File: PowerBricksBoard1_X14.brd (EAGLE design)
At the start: 76.2 x 53.3 mm, 16 parts, among them J1 PESC-02-12-02-01-X-VT-LC(BRIC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

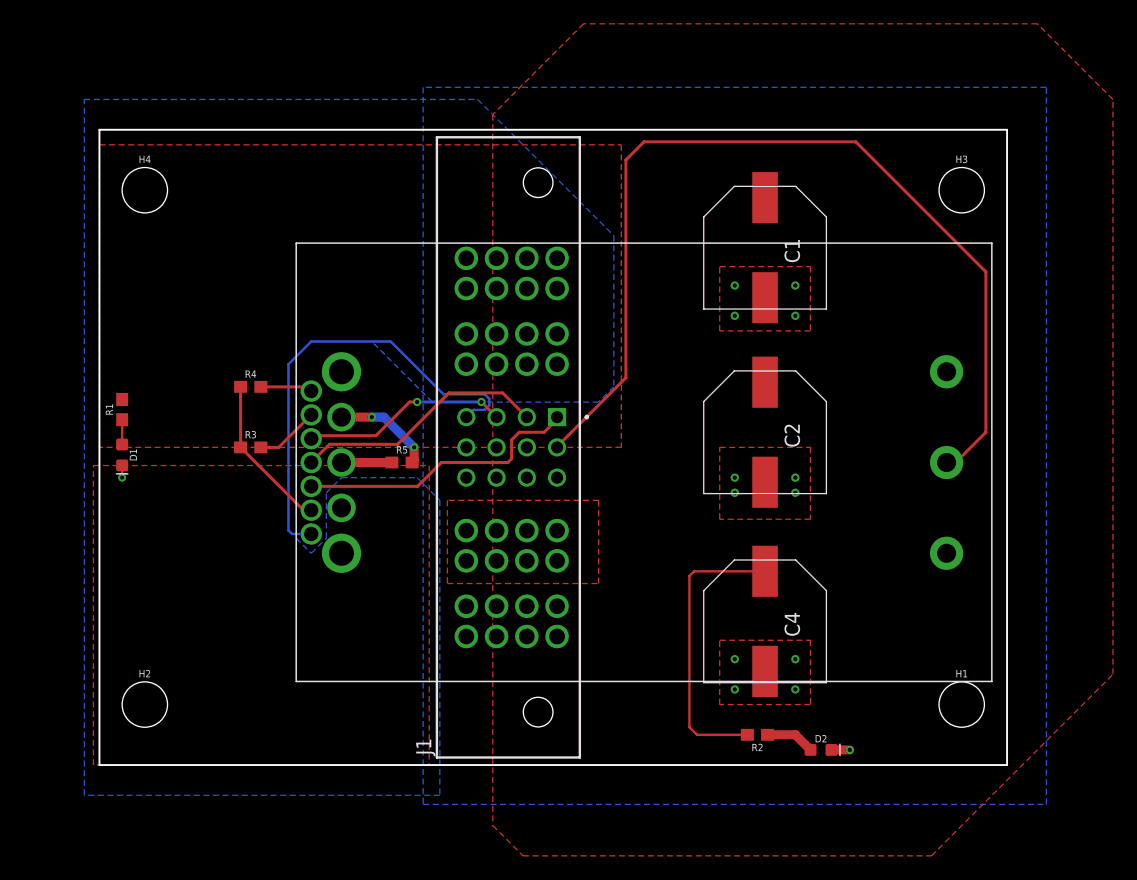
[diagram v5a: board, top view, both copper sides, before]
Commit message: Added Silkscreen
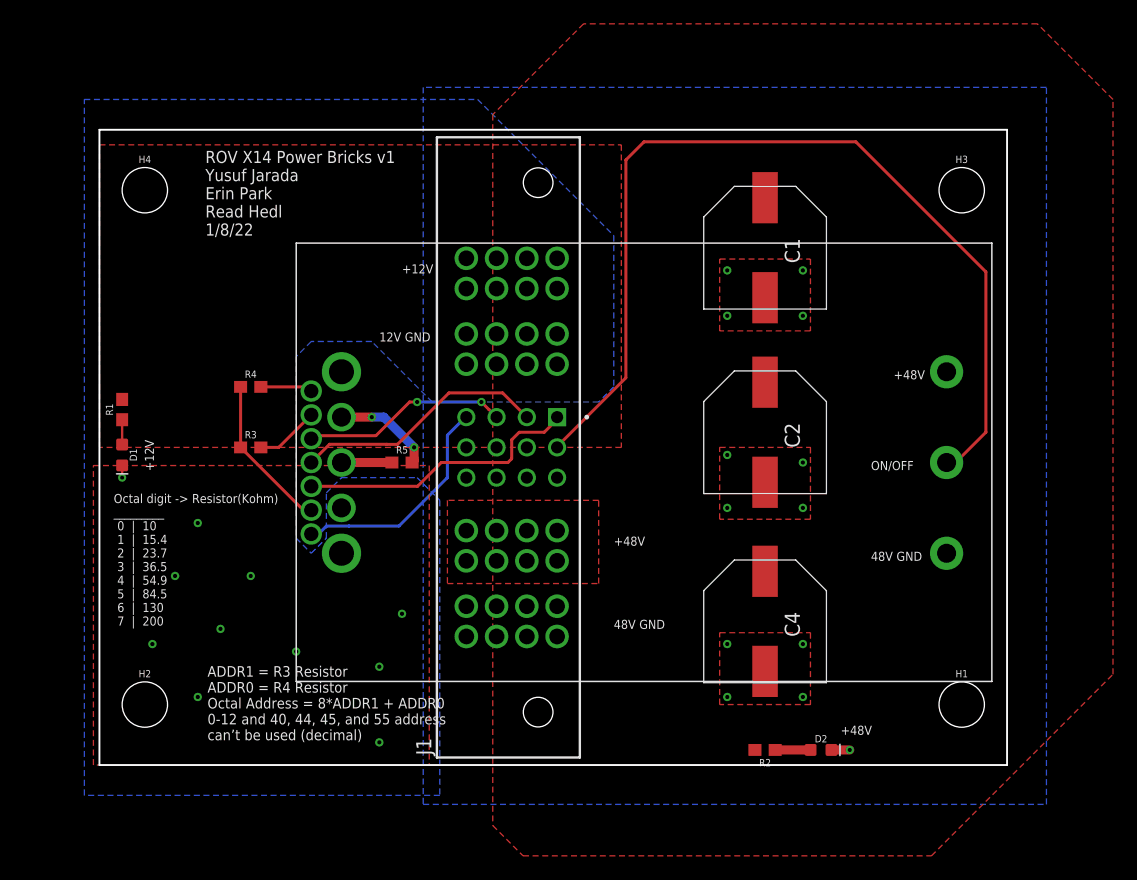
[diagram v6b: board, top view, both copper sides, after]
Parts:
- moved R2 1.42 mm to (55.9, 0.00)
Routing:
- net 48V: track 24.3 -> 0.00 mm
- net C2: track 38.5 -> 19.2 mm
- net N$2: track 4.13 -> 2.97 mm
- net 12_GND: vias 1 -> 11
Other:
- board text added: "+12V"
- board text added: "+48V"
- board text added: "12V GND"
- board text added: "48V GND"
- board text added: "ADDR1 = R3 Resistor ADDR0 = R4 Resistor Octal Address = 8*ADDR1 + ADDR0 0-12 and 40, 44, 45, and 55 address can’t be used (decimal)"
- board text added: "ON/OFF"
- board text added: "Octal digit -> Resistor(Kohm) _________ 0 | 10 1 | 15.4 2 | 23.7 3 | 36.5 4 | 54.9 5 | 84.5 6 | 130 7 | 200"
- board text added: "ROV X14 Power Bricks v1 Yusuf Jarada Erin Park Read Hedl 1/8/22"
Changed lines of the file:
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@@
 <?xml version="1.0" encoding="utf-8"?>
 <!DOCTYPE eagle SYSTEM "eagle.dtd">
-<eagle version="9.6.2">
+<eagle version="9.5.0">
 <drawing>
 <settings>
@@
 <wire x1="76.2" y1="52.07" x2="0" y2="52.07" width="0" layer="20"/>
 <wire x1="0" y1="52.07" x2="0" y2="-1.27" width="0" layer="20"/>
+<text x="8.89" y="43.18" size="1.016" layer="25">ROV X14 Power Bricks v1
+Yusuf Jarada
+Erin Park
+Read Hedl
+1/8/22</text>
+<text x="66.675" y="31.115" size="0.762" layer="25">+48V</text>
+<text x="64.77" y="15.875" size="0.762" layer="25">48V GND</text>
+<text x="64.77" y="23.495" size="0.762" layer="25">ON/OFF</text>
+<text x="25.4" y="40.005" size="0.762" layer="25">+12V</text>
+<text x="43.18" y="17.145" size="0.762" layer="25">+48V</text>
+<text x="43.18" y="10.16" size="0.762" layer="25">48V GND</text>
+<text x="23.495" y="34.29" size="0.762" layer="25">12V GND</text>
+<text x="62.23" y="1.27" size="0.762" layer="25">+48V</text>
+<text x="3.81" y="26.035" size="0.762" layer="25" rot="R270">+12V</text>
+<text x="9.0678" y="0.8128" size="0.889" layer="25">ADDR1 = R3 Resistor
+ADDR0 = R4 Resistor
+Octal Address = 8*ADDR1 + ADDR0
+0-12 and 40, 44, 45, and 55 address
+can’t be used (decimal)</text>
+<text x="1.1938" y="10.4394" size="0.762" layer="25">Octal digit -&gt; Resistor(Kohm)
+_________
+ 0  |  10
+ 1  |  15.4
+ 2  |  23.7
+ 3  |  36.5
+ 4  |  54.9
+ 5  |  84.5
+ 6  |  130
+ 7  |  200</text>
 </plain>
 <attributes>
@@
 <attribute name="VALUE" x="2.667" y="28.575" size="0.6096" layer="27" font="vector" ratio="20" rot="R90" align="top-center"/>
 </element>
-<element name="R2" library="SparkFun-Resistors" library_urn="urn:adsk.eagle:library:532" package="0603" package3d_urn="urn:adsk.eagle:package:39650/1" value="2400" x="55.245" y="1.27" smashed="yes" rot="R180">
-<attribute name="NAME" x="55.245" y="0.508" size="0.6096" layer="25" font="vector" ratio="20" rot="R180" align="bottom-center"/>
-<attribute name="PROD_ID" value=" " x="22.225" y="69.85" size="1.778" layer="27" rot="R180" display="off"/>
-<attribute name="VALUE" x="55.245" y="2.032" size="0.6096" layer="27" font="vector" ratio="20" rot="R180" align="top-center"/>
+<element name="R2" library="SparkFun-Resistors" library_urn="urn:adsk.eagle:library:532" package="0603" package3d_urn="urn:adsk.eagle:package:39650/1" value="2400" x="55.88" y="0" smashed="yes" rot="R180">
+<attribute name="NAME" x="55.88" y="-0.762" size="0.6096" layer="25" font="vector" ratio="20" rot="R180" align="bottom-center"/>
+<attribute name="PROD_ID" value=" " x="22.86" y="68.58" size="1.778" layer="27" rot="R180" display="off"/>
+<attribute name="VALUE" x="55.88" y="0.762" size="0.6096" layer="27" font="vector" ratio="20" rot="R180" align="top-center"/>
 </element>
 <element name="R3" library="SparkFun-Resistors" library_urn="urn:adsk.eagle:library:532" package="0603" package3d_urn="urn:adsk.eagle:package:39650/1" value=" " x="12.7" y="25.4" smashed="yes">
@@
 </polygon>
 <contactref element="U$2" pad="4"/>
-<polygon width="0.254" layer="1">
-<vertex x="52.07" y="9.2075"/>
-<vertex x="59.69" y="9.2075"/>
+<polygon width="0.762" layer="1">
+<vertex x="52.07" y="9.8425"/>
+<vertex x="59.69" y="9.8425"/>
 <vertex x="59.69" y="3.81"/>
 <vertex x="52.07" y="3.81"/>
 </polygon>
-<via x="53.34" y="7.62" extent="1-16" drill="0.35"/>
-<via x="58.42" y="7.62" extent="1-16" drill="0.35"/>
-<polygon width="0.254" layer="1">
-<vertex x="52.07" y="40.5765"/>
-<vertex x="59.69" y="40.5765"/>
+<via x="52.705" y="8.89" extent="1-16" drill="0.35"/>
+<via x="59.055" y="8.89" extent="1-16" drill="0.35"/>
+<polygon width="0.762" layer="1">
+<vertex x="52.07" y="41.2115"/>
+<vertex x="59.69" y="41.2115"/>
 <vertex x="59.69" y="35.179"/>
 <vertex x="52.07" y="35.179"/>
 </polygon>
-<polygon width="0.254" layer="1">
+<polygon width="0.762" layer="1">
 <vertex x="52.07" y="25.4"/>
 <vertex x="59.69" y="25.4"/>
@@
 <vertex x="52.07" y="19.3675"/>
 </polygon>
-<via x="53.34" y="21.59" extent="1-16" drill="0.35"/>
-<via x="58.42" y="21.59" extent="1-16" drill="0.35"/>
-<via x="58.42" y="22.86" extent="1-16" drill="0.35"/>
-<via x="53.34" y="22.86" extent="1-16" drill="0.35"/>
-<via x="53.34" y="36.449" extent="1-16" drill="0.35"/>
-<via x="53.34" y="38.989" extent="1-16" drill="0.35"/>
-<via x="58.42" y="38.989" extent="1-16" drill="0.35"/>
-<via x="58.42" y="36.449" extent="1-16" drill="0.35"/>
-<via x="53.34" y="5.08" extent="1-16" drill="0.35"/>
-<via x="58.42" y="5.08" extent="1-16" drill="0.35"/>
+<via x="52.705" y="20.32" extent="1-16" drill="0.35"/>
+<via x="59.055" y="20.32" extent="1-16" drill="0.35"/>
+<via x="59.055" y="24.13" extent="1-16" drill="0.35"/>
+<via x="52.705" y="24.765" extent="1-16" drill="0.35"/>
+<via x="52.705" y="36.449" extent="1-16" drill="0.35"/>
+<via x="52.705" y="40.259" extent="1-16" drill="0.35"/>
+<via x="59.055" y="40.259" extent="1-16" drill="0.35"/>
+<via x="59.055" y="36.449" extent="1-16" drill="0.35"/>
+<via x="52.705" y="4.445" extent="1-16" drill="0.35"/>
+<via x="59.055" y="4.445" extent="1-16" drill="0.35"/>
 <contactref element="J1" pad="P04_1"/>
 <contactref element="J1" pad="P04_2"/>
@@
 <contactref element="U$2" pad="10"/>
 <contactref element="J1" pad="04"/>
-<wire x1="17.78" y1="18.13" x2="16.16" y2="18.13" width="0.2032" layer="16"/>
-<wire x1="16.16" y1="18.13" x2="15.875" y2="18.415" width="0.2032" layer="16"/>
-<wire x1="15.875" y1="18.415" x2="15.875" y2="32.385" width="0.2032" layer="16"/>
-<wire x1="15.875" y1="32.385" x2="17.78" y2="34.29" width="0.2032" layer="16"/>
-<wire x1="32.3398875" y1="29.8676" x2="32.7251" y2="29.4823875" width="0.2032" layer="16"/>
-<wire x1="32.7251" y1="29.4823875" x2="32.7251" y2="28.9376125" width="0.2032" layer="16"/>
-<wire x1="32.7251" y1="28.9376125" x2="32.3398875" y2="28.5524" width="0.2032" layer="16"/>
-<wire x1="24.45" y1="34.29" x2="28.8724" y2="29.8676" width="0.2032" layer="16"/>
-<wire x1="32.3398875" y1="28.5524" x2="31.4124" y2="28.5524" width="0.2032" layer="16"/>
-<wire x1="31.4124" y1="28.5524" x2="30.8" y2="27.94" width="0.2032" layer="16"/>
-<wire x1="28.8724" y1="29.8676" x2="32.3398875" y2="29.8676" width="0.2032" layer="16"/>
-<wire x1="17.78" y1="34.29" x2="24.45" y2="34.29" width="0.2032" layer="16"/>
+<wire x1="17.78" y1="18.13" x2="18.384" y2="18.13" width="0.254" layer="16"/>
+<wire x1="20.95383125" y1="18.7898" x2="20.96003125" y2="18.796" width="0.254" layer="16"/>
+<wire x1="19.0438" y1="18.7898" x2="20.95383125" y2="18.7898" width="0.254" layer="16"/>
+<wire x1="25.146" y1="18.796" x2="29.21" y2="22.86" width="0.254" layer="16"/>
+<wire x1="29.21" y1="22.86" x2="29.21" y2="26.416" width="0.254" layer="16"/>
+<wire x1="29.21" y1="26.416" x2="30.734" y2="27.94" width="0.254" layer="16"/>
+<wire x1="30.734" y1="27.94" x2="30.8" y2="27.94" width="0.254" layer="16"/>
+<wire x1="18.384" y1="18.13" x2="19.0438" y2="18.7898" width="0.254" layer="16"/>
+<wire x1="20.96003125" y1="18.796" x2="25.146" y2="18.796" width="0.254" layer="16"/>
 </signal>
 <signal name="12_GND">
@@
 <vertex x="27.686" y="-1.27"/>
 </polygon>
+<via x="8.255" y="19.05" extent="1-16" drill="0.35"/>
+<via x="6.35" y="14.605" extent="1-16" drill="0.35"/>
+<via x="12.7" y="14.605" extent="1-16" drill="0.35"/>
+<via x="10.16" y="10.16" extent="1-16" drill="0.35"/>
+<via x="4.445" y="8.89" extent="1-16" drill="0.35"/>
+<via x="8.255" y="4.445" extent="1-16" drill="0.35"/>
+<via x="16.51" y="8.255" extent="1-16" drill="0.35"/>
+<via x="23.495" y="0.635" extent="1-16" drill="0.35"/>
+<via x="23.495" y="6.985" extent="1-16" drill="0.35"/>
+<via x="25.4" y="11.43" extent="1-16" drill="0.35"/>
 </signal>
 <signal name="ALERT">
@@
 <contactref element="D2" pad="A"/>
 <contactref element="R2" pad="1"/>
-<wire x1="58.432" y1="1.27" x2="56.095" y2="1.27" width="0.762" layer="1"/>
-<wire x1="58.432" y1="1.27" x2="59.702" y2="0" width="0.762" layer="1"/>
+<wire x1="56.73" y1="0" x2="59.702" y2="0" width="0.762" layer="1"/>
 </signal>
 <signal name="DGND">
@@
 </polygon>
 <contactref element="U$2" pad="1"/>
-<polygon width="1.016" layer="1" isolate="1.27" rank="4">
+<polygon width="1.016" layer="1" rank="4">
 <vertex x="40.64" y="60.96"/>
 <vertex x="33.02" y="53.34"/>
@@
 <contactref element="J1" pad="P03_3"/>
 <contactref element="J1" pad="P03_4"/>
-<wire x1="54.395" y1="1.27" x2="50.165" y2="1.27" width="0.2032" layer="1"/>
-<wire x1="50.165" y1="1.27" x2="49.53" y2="1.905" width="0.2032" layer="1"/>
-<wire x1="49.53" y1="1.905" x2="49.53" y2="14.605" width="0.2032" layer="1"/>
-<wire x1="49.53" y1="14.605" x2="49.92" y2="14.995" width="0.2032" layer="1"/>
-<wire x1="49.92" y1="14.995" x2="55.88" y2="14.995" width="0.2032" layer="1"/>
 </signal>
 </signals>
@@
 </drawing>
 <compatibility>
+<note version="6.3" minversion="6.2.2" severity="warning">
+Since Version 6.2.2 text objects can contain more than one line,
+which will not be processed correctly with this version.
+</note>
 <note version="8.2" severity="warning">
 Since Version 8.2, EAGLE supports online libraries. The ids
